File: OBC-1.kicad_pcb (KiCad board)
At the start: 2 copper layers, 42.8 x 42.8 mm, 72 parts, among them J1 ERM8-020-X, U11 TMS5701227CZWTQQ1, U3 LTC4353, U4 SN65HVD230M-EP, U5 SN65HVD230M-EP, U6 SN65HVD230M-EP

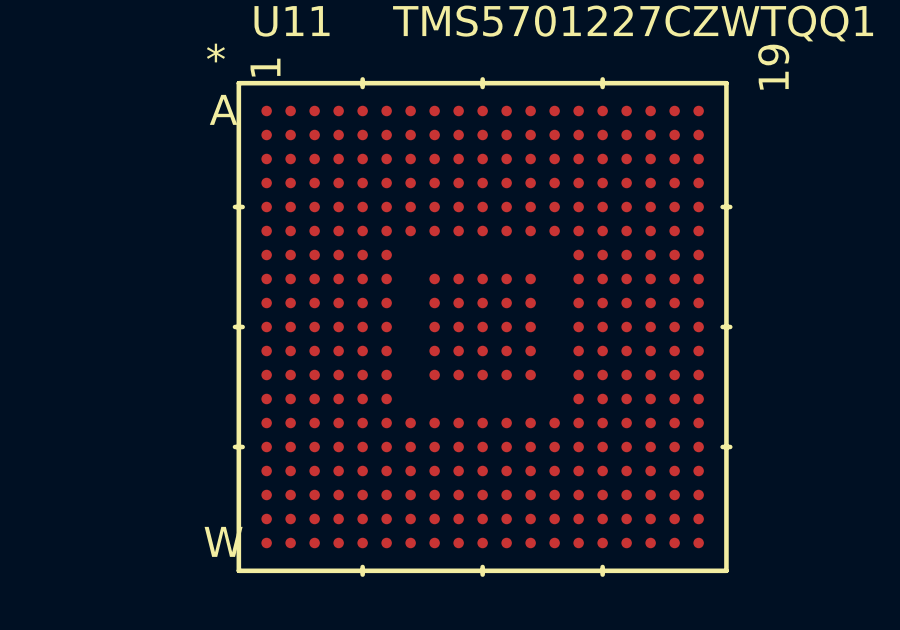
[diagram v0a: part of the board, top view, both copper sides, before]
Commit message: set up PCB stackup and routing design rules, began power planing and power breakouts for the TMS570
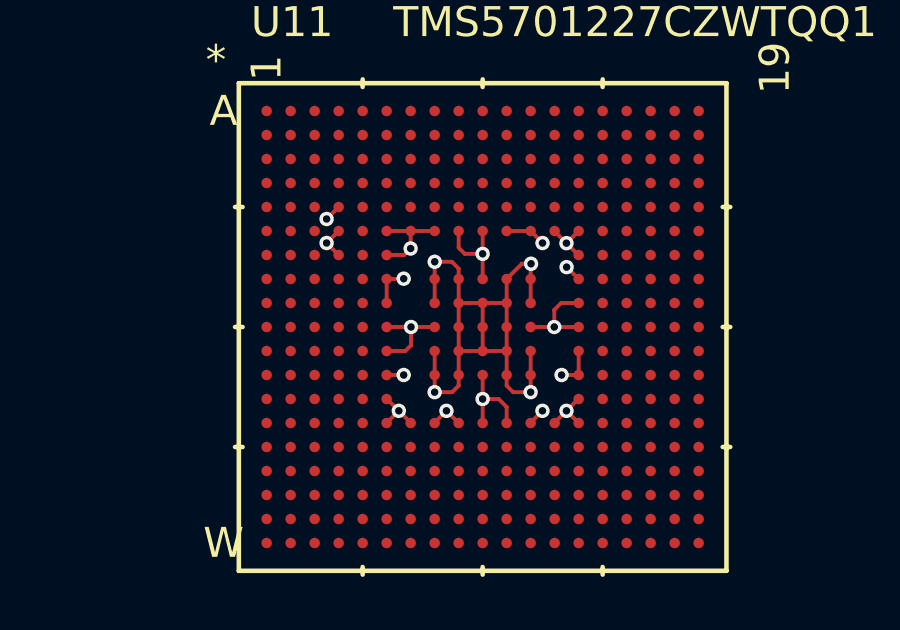
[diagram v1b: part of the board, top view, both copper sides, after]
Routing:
- net GND: track 0.00 -> 23.1 mm, vias 0 -> 6
- net OBC_3V3: track 0.00 -> 15.2 mm, vias 0 -> 11
- net OBC_1V2: track 0.00 -> 12.3 mm, vias 0 -> 4
- added copper zone on In1_GND.Cu, net GND
- added copper zone on In4_GND.Cu, net GND
- added copper zone on In3.Cu, net OBC_1V2
- added copper zone on In3.Cu, net OBC_3V3
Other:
- copper layers 2 -> 6
- net class Default: clearance 0.2 -> 0.15; trace_width 0.25 -> 0.1; via_dia 0.8 -> 0.48; via_drill 0.4 -> 0.25
- rule trace_clearance: 0.2 -> 0.15
- rule trace_min: 0.2 -> 0.1
- rule via_min_drill: 0.3 -> 0.25

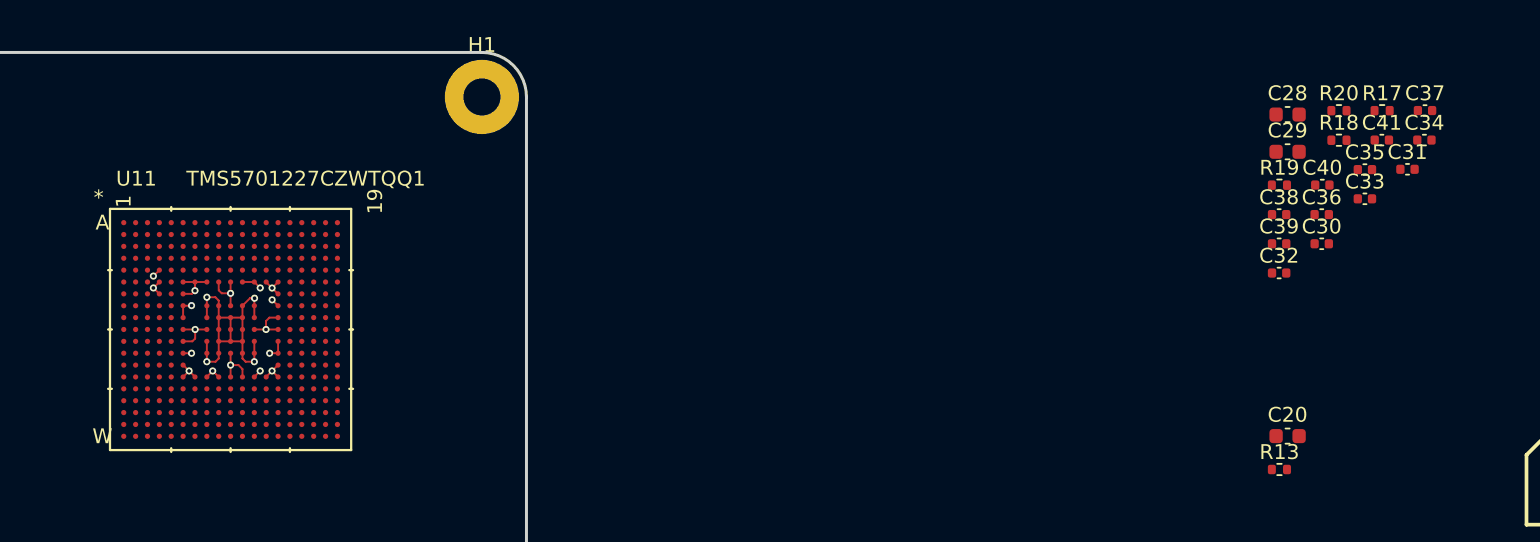
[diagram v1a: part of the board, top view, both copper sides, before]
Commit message: added extra decoupling cap for VCCAD and completed initial routing of TMS570 power breakout and decoupling
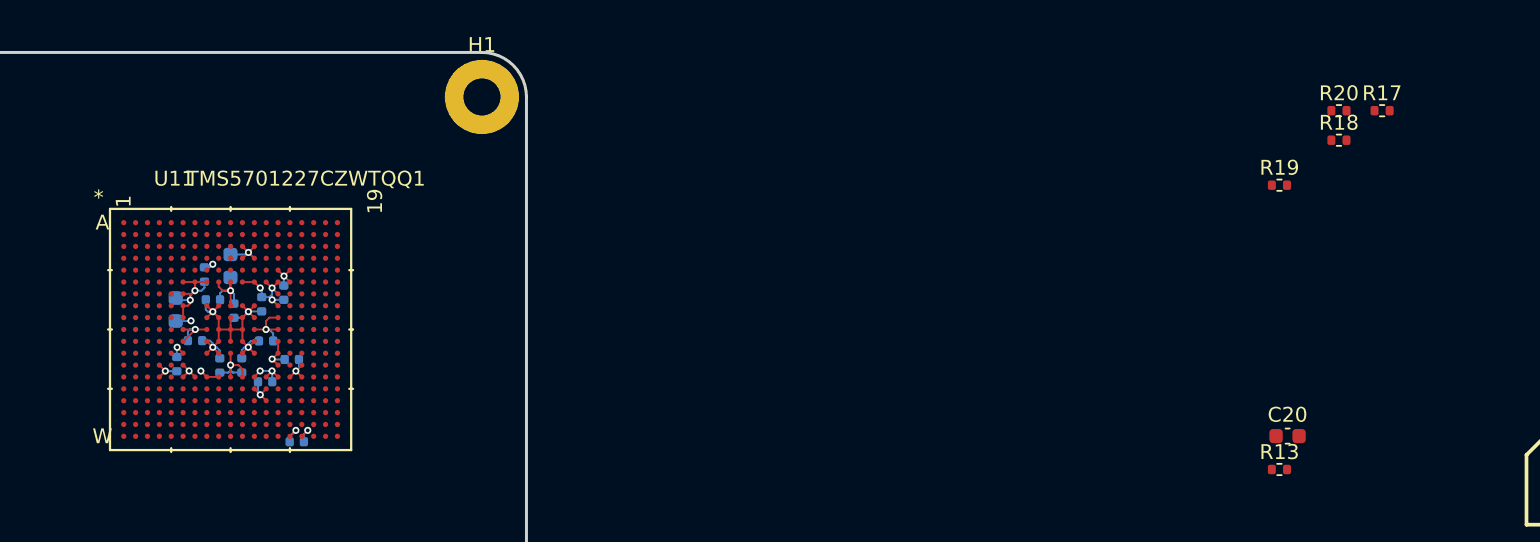
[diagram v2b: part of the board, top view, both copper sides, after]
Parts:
- added C42: 100n-10V-0402-5%-CER, Capacitor_SMD:C_0402_1005Metric, B.Cu at (116.2, 97.7)
- C28, C29, C30, C31, C32, C33, C34, C35, C36, C37, C38, C39, C40, C41: moved to B.Cu
- U11: footprint ZWT337 -> TFT_BGA:ZWT337
- moved C34 82.7 mm to (110.0, 86.5), turned to 90 degrees
- moved C37 82.7 mm to (110.6, 88.2), turned to 180 degrees
- moved C41 81.1 mm to (109.4, 90.9)
- moved C33 78.0 mm to (111.0, 92.6), turned to 90 degrees
- moved C31 76.3 mm to (115.9, 92.2)
- moved C28 76.1 mm to (108.1, 88.8), turned to 270 degrees
- moved C38 75.0 mm to (108.1, 92.5), turned to 270 degrees
- moved C36 73.5 mm to (112.5, 92.6), turned to 90 degrees
- moved C35 73.3 mm to (115.4, 87.7), turned to 90 degrees
- moved C40 72.0 mm to (114.2, 90.9), turned to 180 degrees
- moved C29 71.7 mm to (111.7, 85.9), turned to 90 degrees
- moved C30 71.6 mm to (113.9, 88.5), turned to 270 degrees
- moved C32 70.5 mm to (112.0, 88.9), turned to 270 degrees
- moved C39 69.0 mm to (114.1, 93.7), turned to 180 degrees
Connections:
- J1 pad 30: /TMS570_uC/GPS_STS -> /Connectors/GPS_nRST
- U11 pad A5: /TMS570_uC/GPS_STS -> /Connectors/GPS_STS
- U11 pad B5: /Connectors/GPS_STS -> /Connectors/GPS_nRST
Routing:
- net GND: track 23.1 -> 39.1 mm, vias 6 -> 12
- net OBC_3V3: track 15.2 -> 26.0 mm, vias 11 -> 12
- net OBC_1V2: track 12.3 -> 19.2 mm

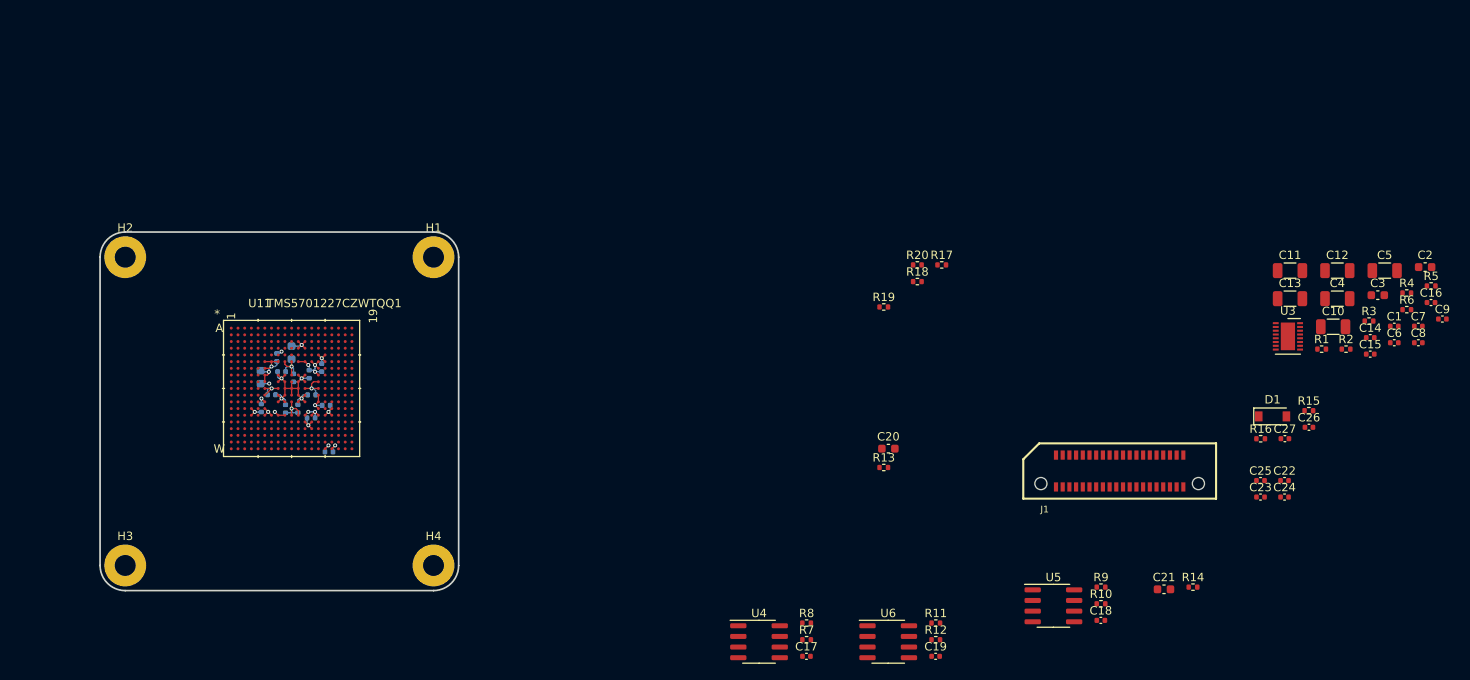
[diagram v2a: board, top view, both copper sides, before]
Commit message: replaced power ORing MOSFETs with lower Rds SOT-23 package
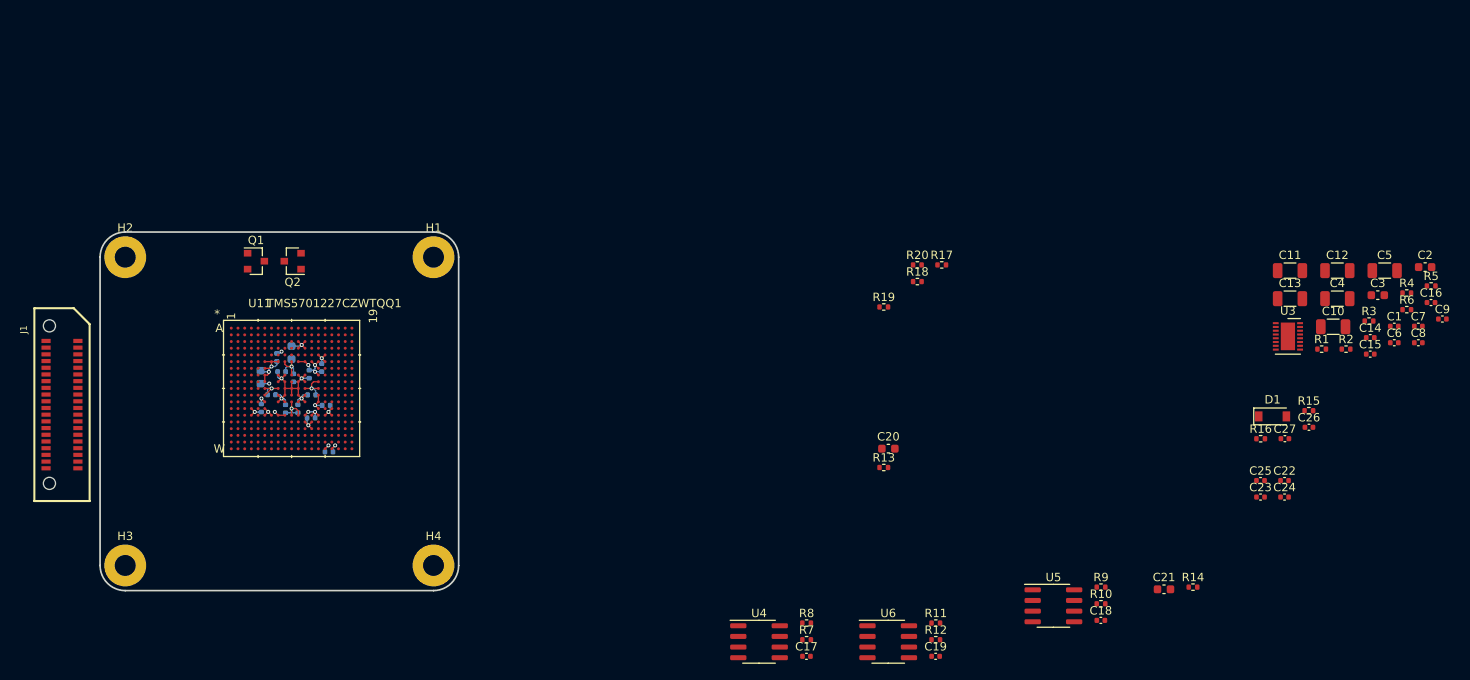
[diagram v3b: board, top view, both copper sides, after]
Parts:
- added Q1: MGSF1N02L, Package_TO_SOT_SMD:SOT-23, F.Cu at (107.5, 75.0)
- added Q2: MGSF1N02L, Package_TO_SOT_SMD:SOT-23, F.Cu at (111.9, 75.0)
- moved J1 126.5 mm to (84.4, 92.1), turned to 270 degrees

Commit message: added new footprints to layout in prep for locating connector positions
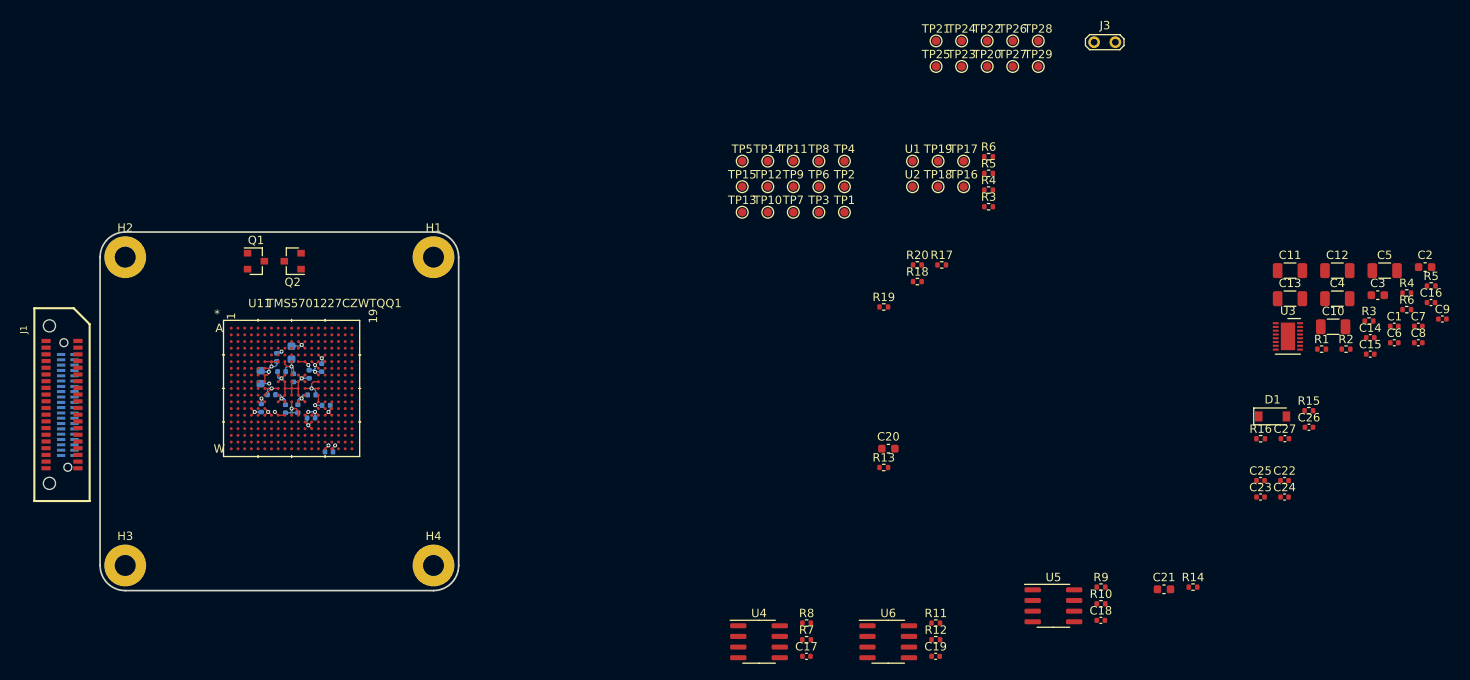
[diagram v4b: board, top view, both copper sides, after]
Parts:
- added J2: ERF6-020-X, TFT_connectors:ERF6-020-XX.X-X-DV-A-XX-K, B.Cu at (85.1, 92.1)
- added J3: Conn_01x02_Female, TFT_TestPoints:TestPoint_2Pads_Pitch2.54mm_Drill0.8mm, F.Cu at (207.5, 48.8)
- added R3: 16K2-50V-0402-1%, Resistor_SMD:R_0402_1005Metric, F.Cu at (195.0, 68.5)
- added R4: 15K-50V-0402-1%, Resistor_SMD:R_0402_1005Metric, F.Cu at (195.0, 66.5)
- added R5: 16K2-50V-0402-1%, Resistor_SMD:R_0402_1005Metric, F.Cu at (195.0, 64.5)
- added R6: 15K-50V-0402-1%, Resistor_SMD:R_0402_1005Metric, F.Cu at (195.0, 62.5)
- added TP1: TEST-POINT, TFT_TestPoints:TestPoint_Pad_D1.0mm, F.Cu at (177.7, 69.1)
- added TP10: TEST-POINT, TFT_TestPoints:TestPoint_Pad_D1.0mm, F.Cu at (168.6, 69.1)
- added TP11: TEST-POINT, TFT_TestPoints:TestPoint_Pad_D1.0mm, F.Cu at (171.6, 63.0)
- added TP12: TEST-POINT, TFT_TestPoints:TestPoint_Pad_D1.0mm, F.Cu at (168.6, 66.1)
- added TP13: TEST-POINT, TFT_TestPoints:TestPoint_Pad_D1.0mm, F.Cu at (165.5, 69.1)
- added TP14: TEST-POINT, TFT_TestPoints:TestPoint_Pad_D1.0mm, F.Cu at (168.6, 63.0)
- added TP15: TEST-POINT, TFT_TestPoints:TestPoint_Pad_D1.0mm, F.Cu at (165.5, 66.1)
- added TP16: TEST-POINT, TFT_TestPoints:TestPoint_Pad_D1.0mm, F.Cu at (192.0, 66.1)
- added TP17: TEST-POINT, TFT_TestPoints:TestPoint_Pad_D1.0mm, F.Cu at (192.0, 63.0)
- added TP18: TEST-POINT, TFT_TestPoints:TestPoint_Pad_D1.0mm, F.Cu at (188.9, 66.1)
- added TP19: TEST-POINT, TFT_TestPoints:TestPoint_Pad_D1.0mm, F.Cu at (188.9, 63.0)
- added TP2: TEST-POINT, TFT_TestPoints:TestPoint_Pad_D1.0mm, F.Cu at (177.7, 66.1)
- added TP20: TEST-POINT, TFT_TestPoints:TestPoint_Pad_D1.0mm, F.Cu at (194.8, 51.7)
- added TP21: TEST-POINT, TFT_TestPoints:TestPoint_Pad_D1.0mm, F.Cu at (188.7, 48.7)
- added TP22: TEST-POINT, TFT_TestPoints:TestPoint_Pad_D1.0mm, F.Cu at (194.8, 48.7)
- added TP23: TEST-POINT, TFT_TestPoints:TestPoint_Pad_D1.0mm, F.Cu at (191.7, 51.7)
- added TP24: TEST-POINT, TFT_TestPoints:TestPoint_Pad_D1.0mm, F.Cu at (191.7, 48.7)
- added TP25: TEST-POINT, TFT_TestPoints:TestPoint_Pad_D1.0mm, F.Cu at (188.7, 51.7)
- added TP26: TEST-POINT, TFT_TestPoints:TestPoint_Pad_D1.0mm, F.Cu at (197.8, 48.7)
- added TP27: TEST-POINT, TFT_TestPoints:TestPoint_Pad_D1.0mm, F.Cu at (197.8, 51.7)
- added TP28: TEST-POINT, TFT_TestPoints:TestPoint_Pad_D1.0mm, F.Cu at (200.9, 48.7)
- added TP29: TEST-POINT, TFT_TestPoints:TestPoint_Pad_D1.0mm, F.Cu at (200.9, 51.7)
- added TP3: TEST-POINT, TFT_TestPoints:TestPoint_Pad_D1.0mm, F.Cu at (174.7, 69.1)
- added TP4: TEST-POINT, TFT_TestPoints:TestPoint_Pad_D1.0mm, F.Cu at (177.7, 63.0)
- added TP5: TEST-POINT, TFT_TestPoints:TestPoint_Pad_D1.0mm, F.Cu at (165.5, 63.0)
- added TP6: TEST-POINT, TFT_TestPoints:TestPoint_Pad_D1.0mm, F.Cu at (174.7, 66.1)
- added TP7: TEST-POINT, TFT_TestPoints:TestPoint_Pad_D1.0mm, F.Cu at (171.6, 69.1)
- added TP8: TEST-POINT, TFT_TestPoints:TestPoint_Pad_D1.0mm, F.Cu at (174.7, 63.0)
- added TP9: TEST-POINT, TFT_TestPoints:TestPoint_Pad_D1.0mm, F.Cu at (171.6, 66.1)
- added U1: TPS62850x-Q1, TFT_TestPoints:TestPoint_Pad_D1.0mm, F.Cu at (185.9, 63.0)
- added U2: TPS62850x-Q1, TFT_TestPoints:TestPoint_Pad_D1.0mm, F.Cu at (185.9, 66.1)
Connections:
- net OBC_1V2 renamed OBC_1V25
- C10 pad 1: OBC_1V2_P -> OBC_1V25_P
- C12 pad 1: OBC_1V2_P -> OBC_1V25_P
- C15 pad 1: OBC_1V2_P -> OBC_1V25_P
- C8 pad 1: OBC_1V2_P -> OBC_1V25_P
- Q2 pad 1: OBC_1V2_P -> OBC_1V25_P
- U11 pad C1: /Power/OBC_1V2_P_PG -> /TMS570_uC/OBC_1V25_P_PG
- U11 pad C2: /Power/OBC_1V2_R_PG -> /TMS570_uC/OBC_1V25_R_PG
- U3 pad 13: OBC_1V2_P -> OBC_1V25_P
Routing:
- added copper zone on In3.Cu, net OBC_1V2
- removed copper zone on In3.Cu, net OBC_1V25
